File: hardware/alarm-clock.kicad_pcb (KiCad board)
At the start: 2 copper layers, 68.6 x 86.4 mm, 41 parts, among them CON1 BARREL_JACK, CON2 BARREL_JACK, IC1 ATMEGA328-P, Q1 Q_NPN_BCE, Q2 Q_NPN_BCE, SW1 SWITCH_INV, SW2 SW_PUSH, SW3 SW_PUSH, U1 LM7805CT, U2 DS1307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

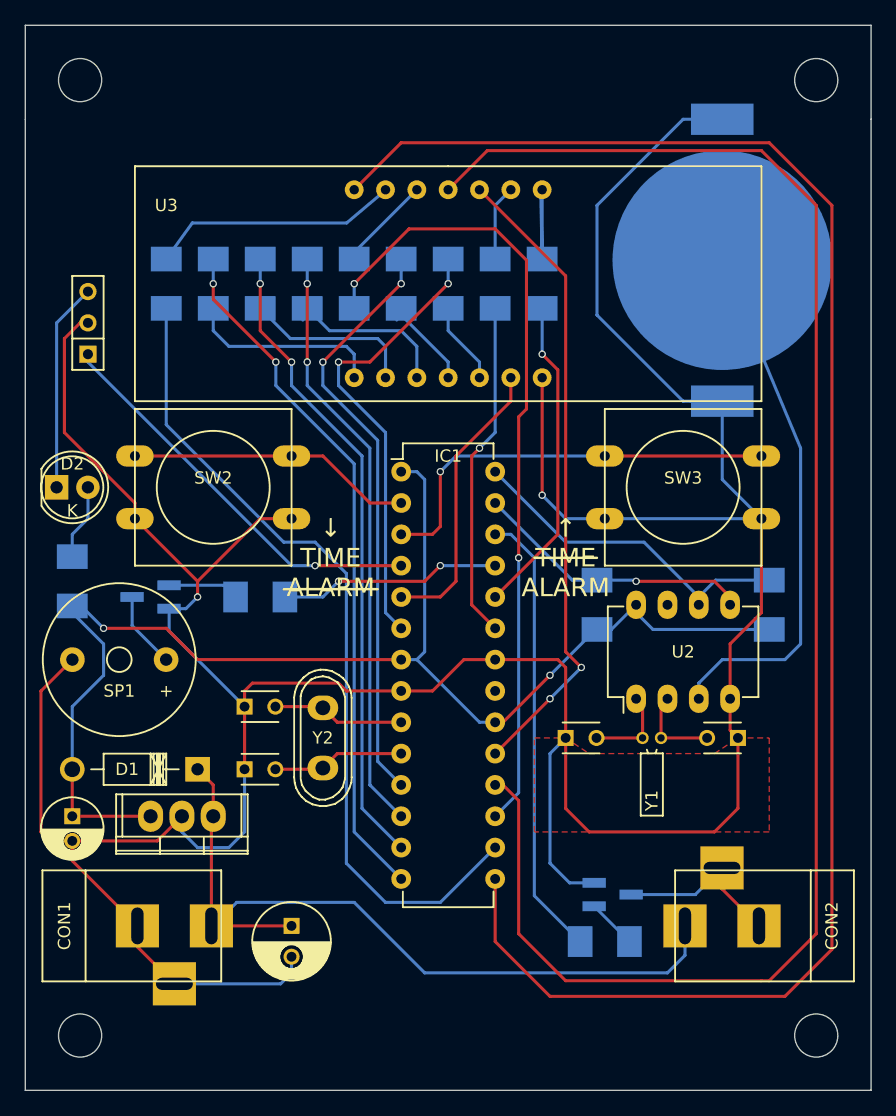
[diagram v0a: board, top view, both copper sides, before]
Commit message: Cleanup and update some footprints
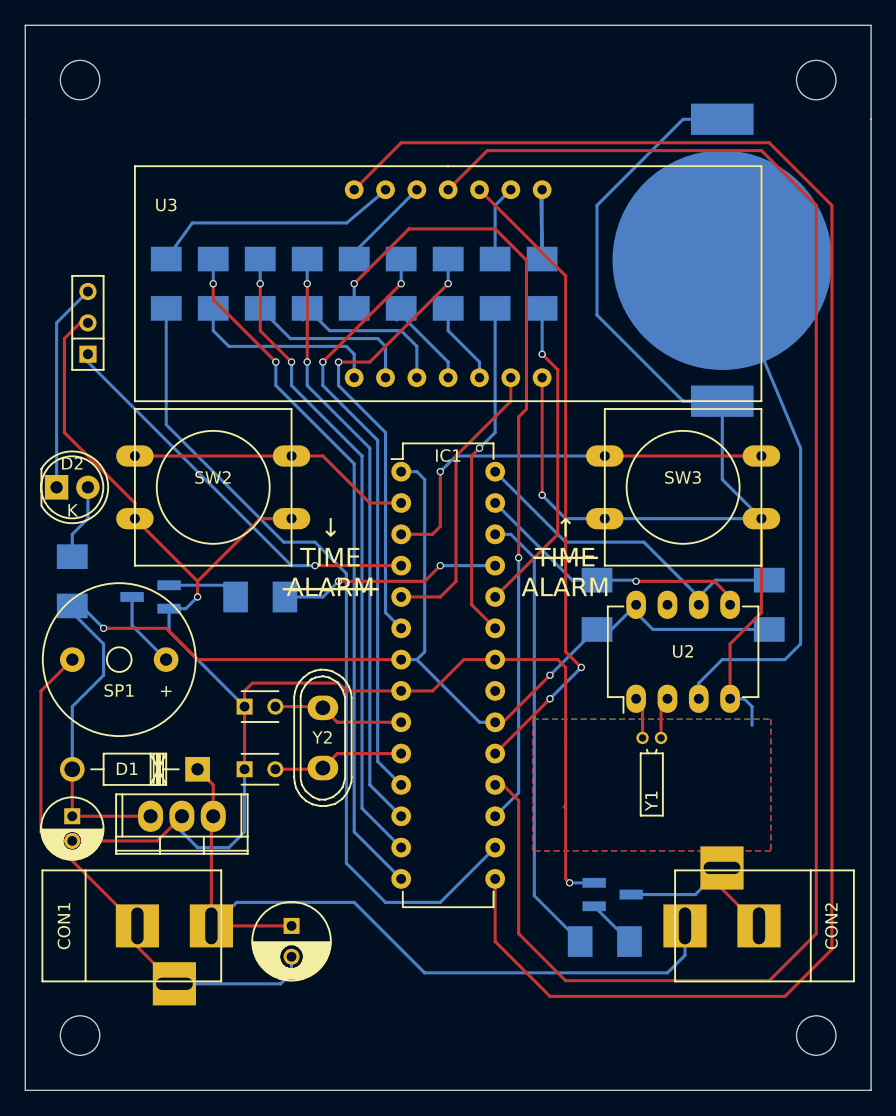
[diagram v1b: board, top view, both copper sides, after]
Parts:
- removed ? (x4): MountingHole_3.5mm, Mounting_Holes:MountingHole_3.5mm
- removed C2, C4: 12.5pF, Capacitors_ThroughHole:C_Disc_D3_P2.5
- added REF**: MountingHole_3.2mm_M3, Mounting_Holes:MountingHole_3.2mm_M3, F.Cu at (178.4, 88.9)
- added REF**: MountingHole_3.2mm_M3, Mounting_Holes:MountingHole_3.2mm_M3, F.Cu at (118.7, 88.9)
- added REF**: MountingHole_3.2mm_M3, Mounting_Holes:MountingHole_3.2mm_M3, F.Cu at (118.7, 166.4)
- added REF**: MountingHole_3.2mm_M3, Mounting_Holes:MountingHole_3.2mm_M3, F.Cu at (178.4, 166.4)
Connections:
- IC1 pad 21: (no net) -> Net-(IC1-Pad21)
- U2 pad 7: (no net) -> Net-(U2-Pad7)
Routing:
- net GND: track 296.3 -> 268.6 mm, vias 2 -> 3
- net Net-(U2-Pad2): track 7.13 -> 3.39 mm
- net Net-(U2-Pad1): track 7.13 -> 3.39 mm
- added copper zone on B.Cu, net GND

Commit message: Add programmer port
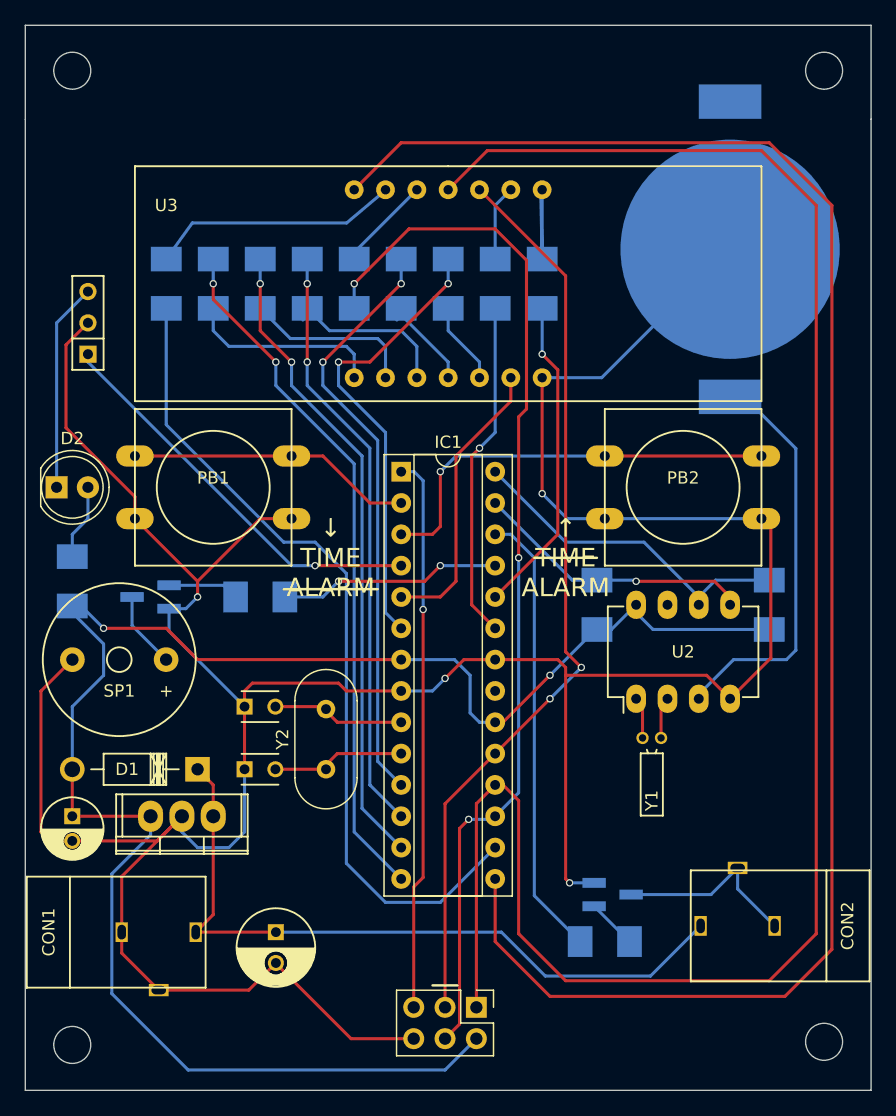
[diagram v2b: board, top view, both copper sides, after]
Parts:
- removed the REF** at (178.4, 88.9)
- removed the REF** at (118.7, 88.9)
- removed the REF** at (118.7, 166.4)
- removed the REF** at (178.4, 166.4)
- removed SW2, SW3: SW_PUSH, Buttons_Switches_ThroughHole:SW_PUSH-12mm
- added P1: PROGRAMMER, Pin_Headers:Pin_Header_Straight_2x03_Pitch2.54mm, F.Cu at (150.9, 164.1)
- added PB1: push_button, Buttons_Switches_THT:SW_PUSH-12mm, F.Cu at (129.5, 121.9)
- added PB2: push_button, Buttons_Switches_THT:SW_PUSH-12mm, F.Cu at (167.6, 121.9)
- added REF**: MountingHole_3mm, Mounting_Holes:MountingHole_3mm, F.Cu at (179.1, 166.9)
- added REF**: MountingHole_3mm, Mounting_Holes:MountingHole_3mm, F.Cu at (118.1, 167.1)
- added REF**: MountingHole_3mm, Mounting_Holes:MountingHole_3mm, F.Cu at (179.1, 88.1)
- added REF**: MountingHole_3mm, Mounting_Holes:MountingHole_3mm, F.Cu at (118.1, 88.1)
- BT1: footprint custom:bat_holder_20mm_smd -> custom:CR2032_SMD
- CON1, CON2: footprint Connectors:BARREL_JACK -> custom:BARREL_JACK
- D2: footprint LEDs:LED-5MM -> LEDs:LED_D5.0mm
- IC1: value ATMEGA328-P -> ATMEGA328P-PU; footprint Housings_DIP:DIP-28_W7.62mm -> Housings_DIP:DIP-28_W7.62mm_Socket
- SW1: value SWITCH_INV -> SPST
- Y2: footprint Crystals:Crystal_HC50-U_Vertical -> Crystals:Crystal_HC49-U_Vertical
- moved Y2 2.55 mm to (138.7, 144.8)
- moved CON1 1.37 mm to (121.9, 158.0)
- moved C1 1.37 mm to (134.6, 158.0)
- moved CON2 1.27 mm to (175.3, 157.5)
- moved BT1 1.09 mm to (171.4, 102.6)
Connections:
- IC1 pad 1: +5V -> RESET
- IC1 pad 21: Net-(IC1-Pad21) -> (no net)
- U2 pad 7: Net-(U2-Pad7) -> (no net)
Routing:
- net RESET: track 0.00 -> 45.1 mm, vias 0 -> 1
- net +5V: track 108.1 -> 141.7 mm
- net PB5: track 52.0 -> 74.3 mm
- net PB3: track 65.6 -> 86.5 mm, vias 2 -> 3
- net PB4: track 132.6 -> 151.2 mm
- net Net-(BT1-Pad1): track 43.2 -> 34.3 mm
- net VPP: track 64.3 -> 58.6 mm
- net Net-(CON2-Pad2): track 14.2 -> 15.5 mm
- net GND: track 268.6 -> 267.4 mm, vias 3 -> 4
- removed copper zone on B.Cu, net GND
- removed copper zone on F.Cu, net GND

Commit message: Add GND fills
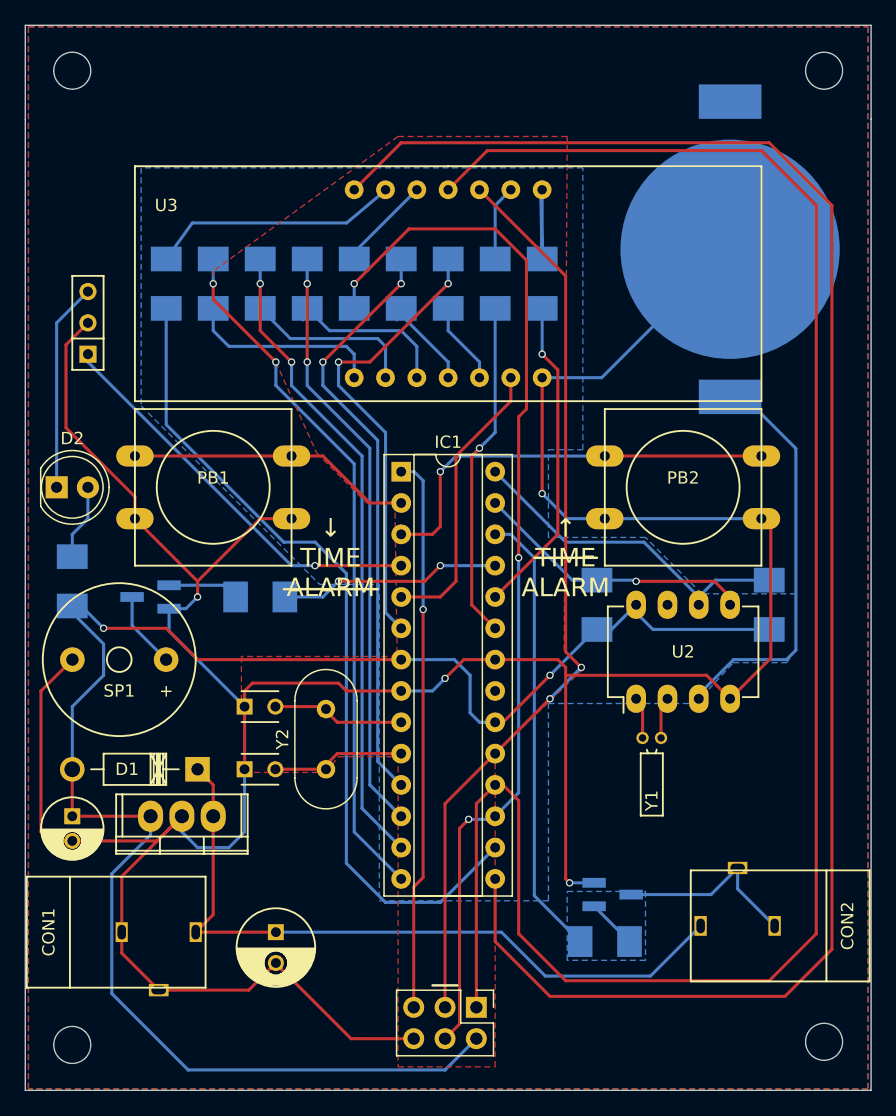
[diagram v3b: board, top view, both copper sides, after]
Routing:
- added copper zone on B.Cu, net GND
- added copper zone on F.Cu, net GND
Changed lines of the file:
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@@
   (general
     (links 85)
-    (no_connects 2)
+    (no_connects 1)
     (area 110.695714 83.163 186.484286 172.207)
     (thickness 1.6)
@@
   (page A4)
   (layers
-    (0 F.Cu signal)
+    (0 F.Cu signal hide)
     (31 B.Cu signal)
     (32 B.Adhes user)
@@
   (segment (start 119.38 111.125) (end 119.38 111.76) (width 0.25) (layer B.Cu) (net 44) (status 30))
   (segment (start 119.38 111.76) (end 135.89 128.27) (width 0.25) (layer B.Cu) (net 44) (status 10))
+  (zone (net 1) (net_name GND) (layer F.Cu) (hatch edge 0.508)
+    (connect_pads (clearance 0.508))
+    (min_thickness 0.254)
+    (fill yes (arc_segments 16) (thermal_gap 0.508) (thermal_bridge_width 0.508))
+    (polygon
+      (pts
+        (xy 182.626 170.688) (xy 114.554 170.688) (xy 114.554 84.582) (xy 182.626 84.582)
+      )
+    )
+    (polygon
+      (pts        (xy 144.526 93.472) (xy 129.54 104.394) (xy 129.54 106.68) (xy 134.62 111.76) (xy 137.922 119.126)
+        (xy 141.986 123.19) (xy 144.272 123.19) (xy 144.4498 135.636) (xy 131.826 135.636) (xy 131.826 139.446)
+        (xy 132.08 139.495161) (xy 132.08 145.034) (xy 138.684 145.034) (xy 139.7 143.764) (xy 144.526 143.764)
+        (xy 144.526 168.91) (xy 152.4 168.91) (xy 152.4 143.51) (xy 159.512 136.652) (xy 157.988 135.128)
+        (xy 158.242 93.472)
+      )
+    )
+  )
+  (zone (net 1) (net_name GND) (layer B.Cu) (hatch edge 0.508)
+    (connect_pads (clearance 0.508))
+    (min_thickness 0.254)
+    (fill yes (arc_segments 16) (thermal_gap 0.508) (thermal_bridge_width 0.508))
+    (polygon
+      (pts
+        (xy 182.626 170.688) (xy 114.554 170.688) (xy 114.554 84.582) (xy 182.626 84.582)
+      )
+    )
+    (polygon
+      (pts        (xy 123.698 96.012) (xy 123.698 115.316) (xy 138.176 129.794) (xy 143.002 129.794) (xy 143.002 155.448)
+        (xy 156.718 155.448) (xy 156.718 139.446) (xy 168.656 139.446) (xy 171.704 136.144) (xy 176.022 136.144)
+        (xy 176.784 135.128) (xy 176.784 130.556) (xy 169.164 130.556) (xy 164.592 125.984) (xy 156.718 125.984)
+        (xy 156.718 118.872) (xy 159.512 118.872) (xy 159.512 96.012)
+      )
+    )
+    (polygon
+      (pts        (xy 164.592 160.274) (xy 158.242 160.274) (xy 158.242 154.686) (xy 164.592 154.686)
+      )
+    )
+  )
 )
